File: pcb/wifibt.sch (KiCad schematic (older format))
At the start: 15 parts, among them Q800 IRLML6402, U800 RTL8723BS

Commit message: pcb: working on sch
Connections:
- net CCM_CLKO2: now reaches R803.2, U800.24 (SUSCLK_IN/GPIO6)
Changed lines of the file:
@@
 U 1 1 5D1E5233
 P 4850 5400
-F 0 "C804" V 4598 5400 50  0000 C CNN
-F 1 "33pF/50V/5%" V 4689 5400 50  0000 C CNN
+F 0 "C804" V 4750 5200 50  0000 C CNN
+F 1 "33pF/50V/5%" V 4750 5600 50  0000 C CNN
 F 2 "" H 4888 5250 50  0001 C CNN
 F 3 "~" H 4850 5400 50  0001 C CNN
@@
 AR Path="/5DB51F59/5D1E5CB8" Ref="R?"  Part="1"
 AR Path="/5D1BA41C/5D1E5CB8" Ref="R802"  Part="1"
-F 0 "R802" V 4150 5300 50  0000 L CNN
-F 1 "0R" V 4250 5350 50  0000 L CNN
+F 0 "R802" V 4250 5150 50  0000 L CNN
+F 1 "0R" V 4250 5450 50  0000 L CNN
 F 2 "" V 4280 5400 50  0001 C CNN
 F 3 "~" H 4350 5400 50  0001 C CNN
@@
 Wire Wire Line
 	6700 2700 6700 3100
+Text GLabel 4700 5200 0    50   Input ~ 0
+CCM_CLKO2
+Wire Wire Line
+	4700 5200 5100 5200
+Connection ~ 5100 5200
 $EndSCHEMATC

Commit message: pcb: finishing sch for r0.1
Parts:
- C800, C802, C804, C805, C806: footprint (none) -> Capacitor_SMD:C_0402_1005Metric
- C801, C803: footprint (none) -> Capacitor_SMD:C_0603_1608Metric
- D800: footprint (none) -> Diode_SMD:D_SOD-523
- R800, R801, R802, R803: footprint (none) -> Resistor_SMD:R_0603_1608Metric
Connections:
- net SAI2_RXD: no longer names the net of U800.25 (PCM_DOUT)
- net SAI2_TXC: no longer names the net of U800.26 (PCM_CLK)
- net SAI2_TXD: no longer names the net of U800.27 (PCM_DIN)
- net SAI2_TXFS: no longer names the net of U800.28 (PCM_SYNC)
- no-connect marks 0 -> 4
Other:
- note added: "Due to I/O voltage constraint,\nheadset profile would not be supported.\nUse A2DP instead."
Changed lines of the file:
@@
 F 0 "C800" H 6815 3496 50  0000 L CNN
 F 1 "100nF" H 6815 3405 50  0000 L CNN
-F 2 "" H 6738 3300 50  0001 C CNN
+F 2 "Capacitor_SMD:C_0402_1005Metric" H 6738 3300 50  0001 C CNN
 F 3 "~" H 6700 3450 50  0001 C CNN
 	1    6700 3450
@@
 F 0 "C801" H 7315 3496 50  0000 L CNN
 F 1 "10uF" H 7315 3405 50  0000 L CNN
-F 2 "" H 7238 3300 50  0001 C CNN
+F 2 "Capacitor_SMD:C_0603_1608Metric" H 7238 3300 50  0001 C CNN
 F 3 "~" H 7200 3450 50  0001 C CNN
 	1    7200 3450
@@
 F 0 "C802" H 7815 3496 50  0000 L CNN
 F 1 "100nF" H 7815 3405 50  0000 L CNN
-F 2 "" H 7738 3300 50  0001 C CNN
+F 2 "Capacitor_SMD:C_0402_1005Metric" H 7738 3300 50  0001 C CNN
 F 3 "~" H 7700 3450 50  0001 C CNN
 	1    7700 3450
@@
 F 0 "C803" H 8315 3496 50  0000 L CNN
 F 1 "10uF" H 8315 3405 50  0000 L CNN
-F 2 "" H 8238 3300 50  0001 C CNN
+F 2 "Capacitor_SMD:C_0603_1608Metric" H 8238 3300 50  0001 C CNN
 F 3 "~" H 8200 3450 50  0001 C CNN
 	1    8200 3450
@@
 $EndComp
 $Comp
-L power:GND #PWR?
+L power:GND #PWR0306
 U 1 1 5D1C6F63
 P 7700 3700
-F 0 "#PWR?" H 7700 3450 50  0001 C CNN
+F 0 "#PWR0306" H 7700 3450 50  0001 C CNN
 F 1 "GND" H 7705 3527 50  0000 C CNN
 F 2 "" H 7700 3700 50  0001 C CNN
@@
 AR Path="/5DB2122B/5D1E0260" Ref="#PWR?"  Part="1"
 AR Path="/5DB51F59/5D1E0260" Ref="#PWR?"  Part="1"
-AR Path="/5D1BA41C/5D1E0260" Ref="#PWR?"  Part="1"
-F 0 "#PWR?" H 6700 1750 50  0001 C CNN
+AR Path="/5D1BA41C/5D1E0260" Ref="#PWR0307"  Part="1"
+F 0 "#PWR0307" H 6700 1750 50  0001 C CNN
 F 1 "+3V3" H 6715 2073 50  0000 C CNN
 F 2 "" H 6700 1900 50  0001 C CNN
@@
 F 0 "R801" H 6270 2496 50  0000 L CNN
 F 1 "10K" H 6270 2405 50  0000 L CNN
-F 2 "" V 6130 2450 50  0001 C CNN
+F 2 "Resistor_SMD:R_0603_1608Metric" V 6130 2450 50  0001 C CNN
 F 3 "~" H 6200 2450 50  0001 C CNN
 	1    6200 2450
@@
 F 0 "R800" H 6270 1996 50  0000 L CNN
 F 1 "100K" H 6270 1905 50  0000 L CNN
-F 2 "" V 6130 1950 50  0001 C CNN
+F 2 "Resistor_SMD:R_0603_1608Metric" V 6130 1950 50  0001 C CNN
 F 3 "~" H 6200 1950 50  0001 C CNN
 	1    6200 1950
@@
 AR Path="/5DB2122B/5D1E027E" Ref="#PWR?"  Part="1"
 AR Path="/5DB51F59/5D1E027E" Ref="#PWR?"  Part="1"
-AR Path="/5D1BA41C/5D1E027E" Ref="#PWR?"  Part="1"
-F 0 "#PWR?" H 6200 2350 50  0001 C CNN
+AR Path="/5D1BA41C/5D1E027E" Ref="#PWR0308"  Part="1"
+F 0 "#PWR0308" H 6200 2350 50  0001 C CNN
 F 1 "GND" H 6205 2427 50  0000 C CNN
 F 2 "" H 6200 2600 50  0001 C CNN
@@
 AR Path="/5DB2122B/5D1E0284" Ref="#PWR?"  Part="1"
 AR Path="/5DB51F59/5D1E0284" Ref="#PWR?"  Part="1"
-AR Path="/5D1BA41C/5D1E0284" Ref="#PWR?"  Part="1"
-F 0 "#PWR?" H 6200 1650 50  0001 C CNN
+AR Path="/5D1BA41C/5D1E0284" Ref="#PWR0309"  Part="1"
+F 0 "#PWR0309" H 6200 1650 50  0001 C CNN
 F 1 "+3V3" H 6215 1973 50  0000 C CNN
 F 2 "" H 6200 1800 50  0001 C CNN
@@
 F 0 "D800" H 5950 1984 50  0000 C CNN
 F 1 "RB521S30T1G" H 5950 2075 50  0000 C CNN
-F 2 "" H 5950 2200 50  0001 C CNN
+F 2 "Diode_SMD:D_SOD-523" H 5950 2200 50  0001 C CNN
 F 3 "~" H 5950 2200 50  0001 C CNN
 	1    5950 2200
@@
 Connection ~ 7700 3600
 $Comp
-L power:GND #PWR?
+L power:GND #PWR0310
 U 1 1 5D1C677C
 P 6700 3700
-F 0 "#PWR?" H 6700 3450 50  0001 C CNN
+F 0 "#PWR0310" H 6700 3450 50  0001 C CNN
 F 1 "GND" H 6705 3527 50  0000 C CNN
 F 2 "" H 6700 3700 50  0001 C CNN
@@
 $EndComp
 $Comp
-L power:GND #PWR?
+L power:GND #PWR0311
 U 1 1 5D1E38E1
 P 6500 3900
-F 0 "#PWR?" H 6500 3650 50  0001 C CNN
+F 0 "#PWR0311" H 6500 3650 50  0001 C CNN
 F 1 "GND" H 6505 3727 50  0000 C CNN
 F 2 "" H 6500 3900 50  0001 C CNN
@@
 F 0 "C804" V 4750 5200 50  0000 C CNN
 F 1 "33pF/50V/5%" V 4750 5600 50  0000 C CNN
-F 2 "" H 4888 5250 50  0001 C CNN
+F 2 "Capacitor_SMD:C_0402_1005Metric" H 4888 5250 50  0001 C CNN
 F 3 "~" H 4850 5400 50  0001 C CNN
 	1    4850 5400
@@
 F 0 "C805" H 4485 5604 50  0000 R CNN
 F 1 "DNP" H 4485 5695 50  0000 R CNN
-F 2 "" H 4638 5500 50  0001 C CNN
+F 2 "Capacitor_SMD:C_0402_1005Metric" H 4638 5500 50  0001 C CNN
 F 3 "~" H 4600 5650 50  0001 C CNN
 	1    4600 5650
@@
 F 0 "R802" V 4250 5150 50  0000 L CNN
 F 1 "0R" V 4250 5450 50  0000 L CNN
-F 2 "" V 4280 5400 50  0001 C CNN
+F 2 "Resistor_SMD:R_0603_1608Metric" V 4280 5400 50  0001 C CNN
 F 3 "~" H 4350 5400 50  0001 C CNN
 	1    4350 5400
@@
 F 0 "C806" H 3985 5604 50  0000 R CNN
 F 1 "DNP" H 3985 5695 50  0000 R CNN
-F 2 "" H 4138 5500 50  0001 C CNN
+F 2 "Capacitor_SMD:C_0402_1005Metric" H 4138 5500 50  0001 C CNN
 F 3 "~" H 4100 5650 50  0001 C CNN
 	1    4100 5650
@@
 $EndComp
 $Comp
-L power:GND #PWR?
+L power:GND #PWR0312
 U 1 1 5D1EA804
 P 3700 5600
-F 0 "#PWR?" H 3700 5350 50  0001 C CNN
+F 0 "#PWR0312" H 3700 5350 50  0001 C CNN
 F 1 "GND" H 3705 5427 50  0000 C CNN
 F 2 "" H 3700 5600 50  0001 C CNN
@@
 $EndComp
 $Comp
-L power:GND #PWR?
+L power:GND #PWR0313
 U 1 1 5D1EAE49
 P 4100 5900
-F 0 "#PWR?" H 4100 5650 50  0001 C CNN
+F 0 "#PWR0313" H 4100 5650 50  0001 C CNN
 F 1 "GND" H 4105 5727 50  0000 C CNN
 F 2 "" H 4100 5900 50  0001 C CNN
@@
 $EndComp
 $Comp
-L power:GND #PWR?
+L power:GND #PWR0314
 U 1 1 5D1EB029
 P 4600 5900
-F 0 "#PWR?" H 4600 5650 50  0001 C CNN
+F 0 "#PWR0314" H 4600 5650 50  0001 C CNN
 F 1 "GND" H 4605 5727 50  0000 C CNN
 F 2 "" H 4600 5900 50  0001 C CNN
@@
 $EndComp
 $Comp
-L power:GND #PWR?
+L power:GND #PWR0315
 U 1 1 5D1EB239
 P 5100 5600
-F 0 "#PWR?" H 5100 5350 50  0001 C CNN
+F 0 "#PWR0315" H 5100 5350 50  0001 C CNN
 F 1 "GND" H 5105 5427 50  0000 C CNN
 F 2 "" H 5100 5600 50  0001 C CNN
@@
 Text GLabel 4700 4900 0    50   Input ~ 0
 AP_WAKE_BT
-Text GLabel 4700 4300 0    50   Output ~ 0
-SAI2_RXD
-Text GLabel 4700 4200 0    50   Input ~ 0
-SAI2_TXD
-Text GLabel 4700 4100 0    50   Input ~ 0
-SAI2_TXC
-Text GLabel 4700 4000 0    50   Input ~ 0
-SAI2_TXFS
 Text GLabel 4700 4500 0    50   Output ~ 0
 UART3_RXD
@@
 Text GLabel 4700 4700 0    50   Input ~ 0
 UART3_RTS
-Wire Wire Line
-	4700 4000 5200 4000
-Wire Wire Line
-	4700 4100 5200 4100
-Wire Wire Line
-	4700 4200 5200 4200
-Wire Wire Line
-	4700 4300 5200 4300
 Wire Wire Line
 	4700 4500 5200 4500
@@
 F 0 "R803" H 5170 2896 50  0000 L CNN
 F 1 "10K" H 5170 2805 50  0000 L CNN
-F 2 "" V 5030 2850 50  0001 C CNN
+F 2 "Resistor_SMD:R_0603_1608Metric" V 5030 2850 50  0001 C CNN
 F 3 "~" H 5100 2850 50  0001 C CNN
 	1    5100 2850
@@
 	4700 5200 5100 5200
 Connection ~ 5100 5200
+NoConn ~ 5200 4000
+NoConn ~ 5200 4100
+NoConn ~ 5200 4200
+NoConn ~ 5200 4300
+Text Notes 3450 4250 0    50   ~ 0
+Due to I/O voltage constraint,\nheadset profile would not be supported.\nUse A2DP instead.
 $EndSCHEMATC

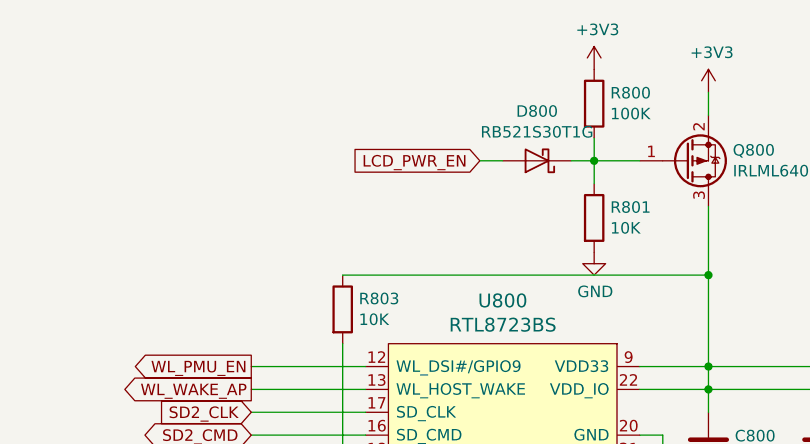
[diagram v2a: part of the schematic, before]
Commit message: pcb: add board outline
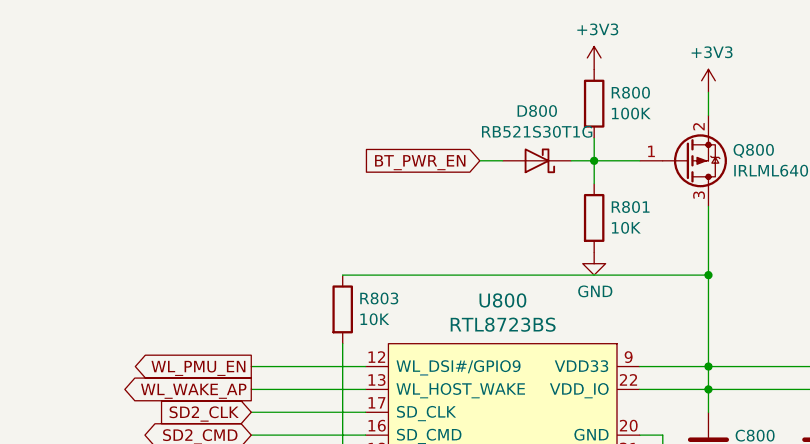
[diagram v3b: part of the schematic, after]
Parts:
- R802: footprint Resistor_SMD:R_0603_1608Metric -> Resistor_SMD:R_0402_1005Metric
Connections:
- net LCD_PWR_EN renamed BT_PWR_EN
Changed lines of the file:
@@
 $EndComp
 Text GLabel 5700 2200 0    50   Input ~ 0
-LCD_PWR_EN
+BT_PWR_EN
 Wire Wire Line
 	6200 2100 6200 2200
@@
 F 0 "R802" V 4250 5150 50  0000 L CNN
 F 1 "0R" V 4250 5450 50  0000 L CNN
-F 2 "Resistor_SMD:R_0603_1608Metric" V 4280 5400 50  0001 C CNN
+F 2 "Resistor_SMD:R_0402_1005Metric" V 4280 5400 50  0001 C CNN
 F 3 "~" H 4350 5400 50  0001 C CNN
 	1    4350 5400

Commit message: pcb: routing
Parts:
- C800, C801, C802, C803, C804, C805, C806: symbol Device:C -> pcb-rescue:C-Device
- D800: symbol Device:D_Schottky -> pcb-rescue:D_Schottky-Device
- Q800: symbol Transistor_FET:IRLML6402 -> pcb-rescue:IRLML6402-Transistor_FET
- R800, R801, R802, R803: symbol Device:R -> pcb-rescue:R-Device
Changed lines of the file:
@@
 $EndComp
 $Comp
-L Device:C C800
+L pcb-rescue:C-Device C800
 U 1 1 5D1C38FE
 P 6700 3450
@@
 $EndComp
 $Comp
-L Device:C C801
+L pcb-rescue:C-Device C801
 U 1 1 5D1C53ED
 P 7200 3450
@@
 $EndComp
 $Comp
-L Device:C C802
+L pcb-rescue:C-Device C802
 U 1 1 5D1C595A
 P 7700 3450
@@
 $EndComp
 $Comp
-L Device:C C803
+L pcb-rescue:C-Device C803
 U 1 1 5D1C5D04
 P 8200 3450
@@
 $EndComp
 $Comp
-L power:GND #PWR0306
+L pcb-rescue:GND-power #PWR0306
 U 1 1 5D1C6F63
 P 7700 3700
@@
 $EndComp
 $Comp
-L power:+3V3 #PWR?
+L pcb-rescue:+3V3-power #PWR?
 U 1 1 5D1E0260
 P 6700 1900
@@
 $EndComp
 $Comp
-L Transistor_FET:IRLML6402 Q?
+L pcb-rescue:IRLML6402-Transistor_FET Q?
 U 1 1 5D1E0266
 P 6600 2200
@@
 	6700 1900 6700 2000
 $Comp
-L Device:R R?
+L pcb-rescue:R-Device R?
 U 1 1 5D1E026D
 P 6200 2450
@@
 $EndComp
 $Comp
-L Device:R R?
+L pcb-rescue:R-Device R?
 U 1 1 5D1E0273
 P 6200 1950
@@
 	6200 2300 6200 2200
 $Comp
-L power:GND #PWR?
+L pcb-rescue:GND-power #PWR?
 U 1 1 5D1E027E
 P 6200 2600
@@
 $EndComp
 $Comp
-L power:+3V3 #PWR?
+L pcb-rescue:+3V3-power #PWR?
 U 1 1 5D1E0284
 P 6200 1800
@@
 $EndComp
 $Comp
-L Device:D_Schottky D?
+L pcb-rescue:D_Schottky-Device D?
 U 1 1 5D1E028A
 P 5950 2200
@@
 Connection ~ 7700 3600
 $Comp
-L power:GND #PWR0310
+L pcb-rescue:GND-power #PWR0310
 U 1 1 5D1C677C
 P 6700 3700
@@
 $EndComp
 $Comp
-L power:GND #PWR0311
+L pcb-rescue:GND-power #PWR0311
 U 1 1 5D1E38E1
 P 6500 3900
@@
 	6500 3500 6500 3600
 $Comp
-L Device:C C804
+L pcb-rescue:C-Device C804
 U 1 1 5D1E5233
 P 4850 5400
@@
 $EndComp
 $Comp
-L Device:C C805
+L pcb-rescue:C-Device C805
 U 1 1 5D1E5893
 P 4600 5650
@@
 $EndComp
 $Comp
-L Device:R R?
+L pcb-rescue:R-Device R?
 U 1 1 5D1E5CB8
 P 4350 5400
@@
 $EndComp
 $Comp
-L Device:C C806
+L pcb-rescue:C-Device C806
 U 1 1 5D1E62F9
 P 4100 5650
@@
 $EndComp
 $Comp
-L power:GND #PWR0312
+L pcb-rescue:GND-power #PWR0312
 U 1 1 5D1EA804
 P 3700 5600
@@
 $EndComp
 $Comp
-L power:GND #PWR0313
+L pcb-rescue:GND-power #PWR0313
 U 1 1 5D1EAE49
 P 4100 5900
@@
 $EndComp
 $Comp
-L power:GND #PWR0314
+L pcb-rescue:GND-power #PWR0314
 U 1 1 5D1EB029
 P 4600 5900
@@
 $EndComp
 $Comp
-L power:GND #PWR0315
+L pcb-rescue:GND-power #PWR0315
 U 1 1 5D1EB239
 P 5100 5600
@@
 	4700 3800 5200 3800
 $Comp
-L Device:R R?
+L pcb-rescue:R-Device R?
 U 1 1 5D20325E
 P 5100 2850

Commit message: pcb: rev 0.1
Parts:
- C800, C801, C802, C803, C804, C805, C806: symbol pcb-rescue:C-Device -> pcb-rescue:C-Device-pcb-rescue
- D800: symbol pcb-rescue:D_Schottky-Device -> pcb-rescue:D_Schottky-Device-pcb-rescue
- Q800: symbol pcb-rescue:IRLML6402-Transistor_FET -> pcb-rescue:IRLML6402-Transistor_FET-pcb-rescue
- R800, R801, R802, R803: symbol pcb-rescue:R-Device -> pcb-rescue:R-Device-pcb-rescue
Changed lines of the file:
@@
 encoding utf-8
 Sheet 11 11
-Title "WiFi & BT"
-Date ""
+Title "RhythmPocket"
+Date "2019-07-16"
 Rev "R0.1"
 Comp "ZephRay"
@@
 $EndComp
 $Comp
-L pcb-rescue:C-Device C800
+L pcb-rescue:C-Device-pcb-rescue C800
 U 1 1 5D1C38FE
 P 6700 3450
@@
 $EndComp
 $Comp
-L pcb-rescue:C-Device C801
+L pcb-rescue:C-Device-pcb-rescue C801
 U 1 1 5D1C53ED
 P 7200 3450
@@
 $EndComp
 $Comp
-L pcb-rescue:C-Device C802
+L pcb-rescue:C-Device-pcb-rescue C802
 U 1 1 5D1C595A
 P 7700 3450
@@
 $EndComp
 $Comp
-L pcb-rescue:C-Device C803
+L pcb-rescue:C-Device-pcb-rescue C803
 U 1 1 5D1C5D04
 P 8200 3450
@@
 $EndComp
 $Comp
-L pcb-rescue:GND-power #PWR0306
+L pcb-rescue:GND-power-pcb-rescue #PWR0306
 U 1 1 5D1C6F63
 P 7700 3700
@@
 $EndComp
 $Comp
-L pcb-rescue:+3V3-power #PWR?
+L pcb-rescue:+3V3-power-pcb-rescue #PWR?
 U 1 1 5D1E0260
 P 6700 1900
@@
 $EndComp
 $Comp
-L pcb-rescue:IRLML6402-Transistor_FET Q?
+L pcb-rescue:IRLML6402-Transistor_FET-pcb-rescue Q?
 U 1 1 5D1E0266
 P 6600 2200
@@
 	6700 1900 6700 2000
 $Comp
-L pcb-rescue:R-Device R?
+L pcb-rescue:R-Device-pcb-rescue R?
 U 1 1 5D1E026D
 P 6200 2450
@@
 $EndComp
 $Comp
-L pcb-rescue:R-Device R?
+L pcb-rescue:R-Device-pcb-rescue R?
 U 1 1 5D1E0273
 P 6200 1950
@@
 	6200 2300 6200 2200
 $Comp
-L pcb-rescue:GND-power #PWR?
+L pcb-rescue:GND-power-pcb-rescue #PWR?
 U 1 1 5D1E027E
 P 6200 2600
@@
 $EndComp
 $Comp
-L pcb-rescue:+3V3-power #PWR?
+L pcb-rescue:+3V3-power-pcb-rescue #PWR?
 U 1 1 5D1E0284
 P 6200 1800
@@
 $EndComp
 $Comp
-L pcb-rescue:D_Schottky-Device D?
+L pcb-rescue:D_Schottky-Device-pcb-rescue D?
 U 1 1 5D1E028A
 P 5950 2200
@@
 Connection ~ 7700 3600
 $Comp
-L pcb-rescue:GND-power #PWR0310
+L pcb-rescue:GND-power-pcb-rescue #PWR0310
 U 1 1 5D1C677C
 P 6700 3700
@@
 $EndComp
 $Comp
-L pcb-rescue:GND-power #PWR0311
+L pcb-rescue:GND-power-pcb-rescue #PWR0311
 U 1 1 5D1E38E1
 P 6500 3900
@@
 	6500 3500 6500 3600
 $Comp
-L pcb-rescue:C-Device C804
+L pcb-rescue:C-Device-pcb-rescue C804
 U 1 1 5D1E5233
 P 4850 5400
@@
 $EndComp
 $Comp
-L pcb-rescue:C-Device C805
+L pcb-rescue:C-Device-pcb-rescue C805
 U 1 1 5D1E5893
 P 4600 5650
@@
 $EndComp
 $Comp
-L pcb-rescue:R-Device R?
+L pcb-rescue:R-Device-pcb-rescue R?
 U 1 1 5D1E5CB8
 P 4350 5400
@@
 $EndComp
 $Comp
-L pcb-rescue:C-Device C806
+L pcb-rescue:C-Device-pcb-rescue C806
 U 1 1 5D1E62F9
 P 4100 5650
@@
 $EndComp
 $Comp
-L pcb-rescue:GND-power #PWR0312
+L pcb-rescue:GND-power-pcb-rescue #PWR0312
 U 1 1 5D1EA804
 P 3700 5600
@@
 $EndComp
 $Comp
-L pcb-rescue:GND-power #PWR0313
+L pcb-rescue:GND-power-pcb-rescue #PWR0313
 U 1 1 5D1EAE49
 P 4100 5900
@@
 $EndComp
 $Comp
-L pcb-rescue:GND-power #PWR0314
+L pcb-rescue:GND-power-pcb-rescue #PWR0314
 U 1 1 5D1EB029
 P 4600 5900
@@
 $EndComp
 $Comp
-L pcb-rescue:GND-power #PWR0315
+L pcb-rescue:GND-power-pcb-rescue #PWR0315
 U 1 1 5D1EB239
 P 5100 5600
@@
 	4700 3800 5200 3800
 $Comp
-L pcb-rescue:R-Device R?
+L pcb-rescue:R-Device-pcb-rescue R?
 U 1 1 5D20325E
 P 5100 2850
